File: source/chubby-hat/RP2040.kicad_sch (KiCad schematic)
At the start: 23 parts, among them U4 P25Q40H-SSH-IT, U5 RP2040, Y1 12M

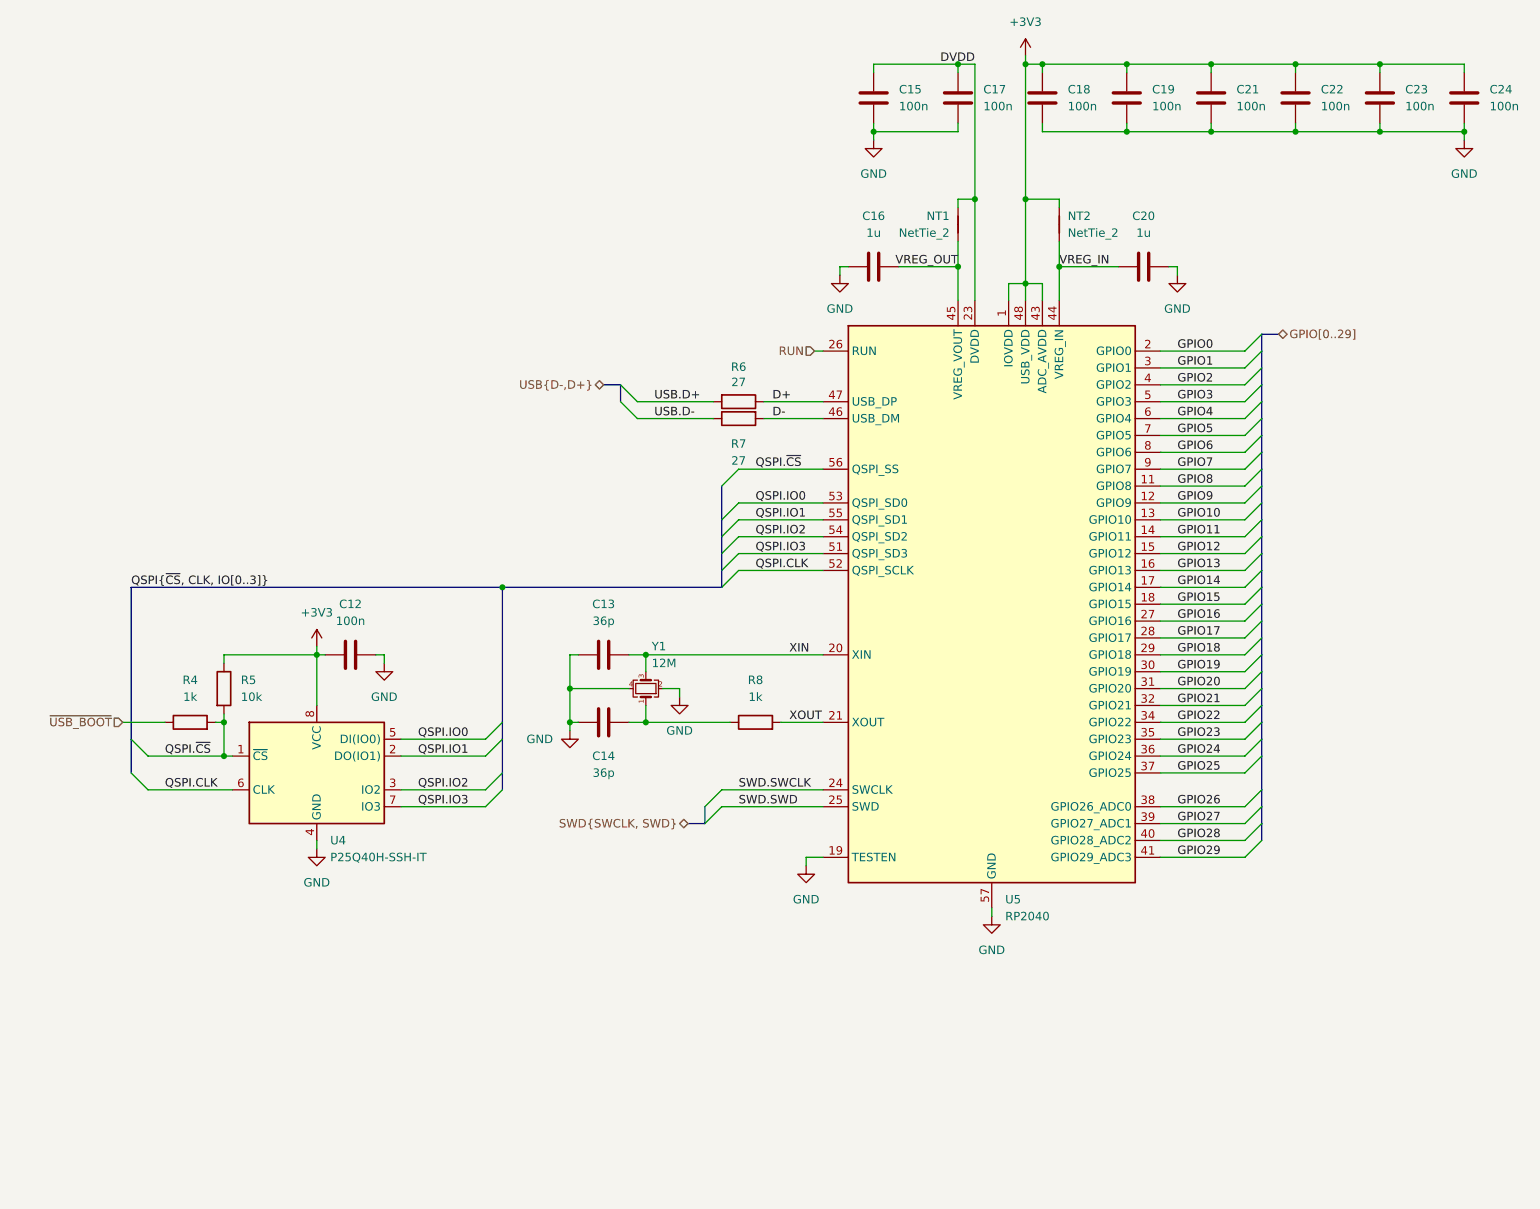
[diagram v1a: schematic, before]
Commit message: add test points and leds - closes #1; add fuse - closes #4; add silk screen art
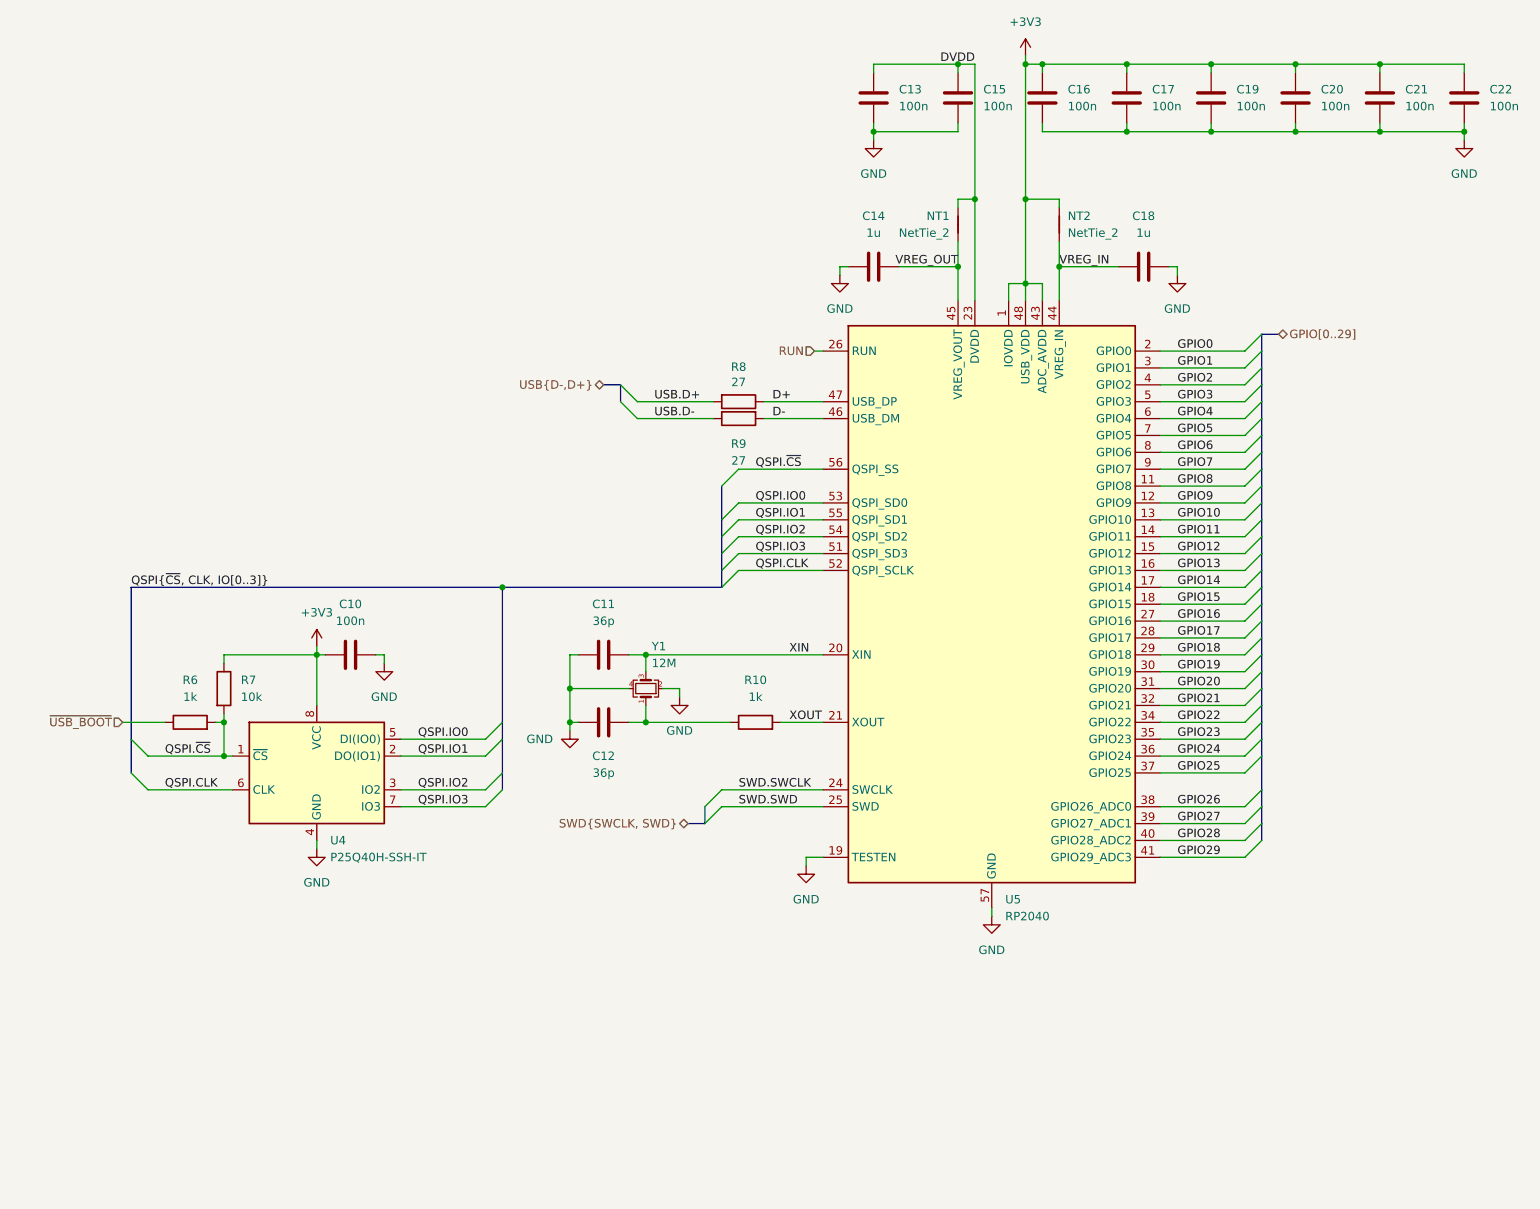
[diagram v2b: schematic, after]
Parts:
- renumbered C12 to C10, C13 to C11, C14 to C12, C15 to C13, C16 to C14, C17 to C15, C18 to C16, C19 to C17, C20 to C18, C21 to C19, C22 to C20, C23 to C21, C24 to C22, R8 to R10, R4 to R6, R5 to R7, R6 to R8, R7 to R9
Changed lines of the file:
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@@
   (symbol (lib_id "power:GND") (at 241.3 36.83 0) (unit 1)
     (in_bom yes) (on_board yes) (fields_autoplaced)
-    (property "Reference" "#PWR093" (id 0) (at 241.3 43.18 0)
+    (property "Reference" "#PWR096" (id 0) (at 241.3 43.18 0)
       (effects (font (size 1.27 1.27)) hide)
     )
@@
   (symbol (lib_id "Device:C") (at 73.66 114.3 90) (unit 1)
     (in_bom yes) (on_board yes) (fields_autoplaced)
-    (property "Reference" "C12" (id 0) (at 73.66 106.68 90))
+    (property "Reference" "C10" (id 0) (at 73.66 106.68 90))
     (property "Value" "100n" (id 1) (at 73.66 109.22 90))
     (property "Footprint" "Capacitor_SMD:C_0603_1608Metric" (id 2) (at 77.47 113.335 0)
@@
   (symbol (lib_id "Device:C") (at 152.4 30.48 0) (unit 1)
     (in_bom yes) (on_board yes) (fields_autoplaced)
-    (property "Reference" "C15" (id 0) (at 156.21 29.2099 0)
+    (property "Reference" "C13" (id 0) (at 156.21 29.2099 0)
       (effects (font (size 1.27 1.27)) (justify left))
     )
@@
   (symbol (lib_id "Device:C") (at 190.5 30.48 0) (unit 1)
     (in_bom yes) (on_board yes) (fields_autoplaced)
-    (property "Reference" "C19" (id 0) (at 194.31 29.2099 0)
+    (property "Reference" "C17" (id 0) (at 194.31 29.2099 0)
       (effects (font (size 1.27 1.27)) (justify left))
     )
@@
   (symbol (lib_id "power:+3V3") (at 68.58 113.03 0) (unit 1)
     (in_bom yes) (on_board yes) (fields_autoplaced)
-    (property "Reference" "#PWR082" (id 0) (at 68.58 116.84 0)
+    (property "Reference" "#PWR085" (id 0) (at 68.58 116.84 0)
       (effects (font (size 1.27 1.27)) hide)
     )
@@
   (symbol (lib_id "power:GND") (at 68.58 143.51 0) (unit 1)
     (in_bom yes) (on_board yes) (fields_autoplaced)
-    (property "Reference" "#PWR083" (id 0) (at 68.58 149.86 0)
+    (property "Reference" "#PWR086" (id 0) (at 68.58 149.86 0)
       (effects (font (size 1.27 1.27)) hide)
     )
@@
   (symbol (lib_id "power:GND") (at 147.32 57.15 0) (unit 1)
     (in_bom yes) (on_board yes) (fields_autoplaced)
-    (property "Reference" "#PWR088" (id 0) (at 147.32 63.5 0)
+    (property "Reference" "#PWR091" (id 0) (at 147.32 63.5 0)
       (effects (font (size 1.27 1.27)) hide)
     )
@@
   (symbol (lib_id "Device:C") (at 228.6 30.48 0) (unit 1)
     (in_bom yes) (on_board yes) (fields_autoplaced)
-    (property "Reference" "C23" (id 0) (at 232.41 29.2099 0)
+    (property "Reference" "C21" (id 0) (at 232.41 29.2099 0)
       (effects (font (size 1.27 1.27)) (justify left))
     )
@@
   (symbol (lib_id "power:GND") (at 152.4 36.83 0) (unit 1)
     (in_bom yes) (on_board yes) (fields_autoplaced)
-    (property "Reference" "#PWR089" (id 0) (at 152.4 43.18 0)
+    (property "Reference" "#PWR092" (id 0) (at 152.4 43.18 0)
       (effects (font (size 1.27 1.27)) hide)
     )
@@
   (symbol (lib_id "power:GND") (at 78.74 115.57 0) (unit 1)
     (in_bom yes) (on_board yes) (fields_autoplaced)
-    (property "Reference" "#PWR084" (id 0) (at 78.74 121.92 0)
+    (property "Reference" "#PWR087" (id 0) (at 78.74 121.92 0)
       (effects (font (size 1.27 1.27)) hide)
     )
@@
   (symbol (lib_id "Device:R") (at 49.53 124.46 90) (unit 1)
     (in_bom yes) (on_board yes) (fields_autoplaced)
-    (property "Reference" "R4" (id 0) (at 49.53 118.11 90))
+    (property "Reference" "R6" (id 0) (at 49.53 118.11 90))
     (property "Value" "1k" (id 1) (at 49.53 120.65 90))
     (property "Footprint" "Resistor_SMD:R_0603_1608Metric" (id 2) (at 49.53 126.238 90)
@@
   (symbol (lib_id "Device:C") (at 203.2 30.48 0) (unit 1)
     (in_bom yes) (on_board yes) (fields_autoplaced)
-    (property "Reference" "C21" (id 0) (at 207.01 29.2099 0)
+    (property "Reference" "C19" (id 0) (at 207.01 29.2099 0)
       (effects (font (size 1.27 1.27)) (justify left))
     )
@@
   (symbol (lib_id "power:+3V3") (at 175.26 24.13 0) (unit 1)
     (in_bom yes) (on_board yes) (fields_autoplaced)
-    (property "Reference" "#PWR091" (id 0) (at 175.26 27.94 0)
+    (property "Reference" "#PWR094" (id 0) (at 175.26 27.94 0)
       (effects (font (size 1.27 1.27)) hide)
     )
@@
   (symbol (lib_id "Device:C") (at 241.3 30.48 0) (unit 1)
     (in_bom yes) (on_board yes) (fields_autoplaced)
-    (property "Reference" "C24" (id 0) (at 245.11 29.2099 0)
+    (property "Reference" "C22" (id 0) (at 245.11 29.2099 0)
       (effects (font (size 1.27 1.27)) (justify left))
     )
@@
   (symbol (lib_id "Device:C") (at 152.4 55.88 270) (unit 1)
     (in_bom yes) (on_board yes) (fields_autoplaced)
-    (property "Reference" "C16" (id 0) (at 152.4 48.26 90))
+    (property "Reference" "C14" (id 0) (at 152.4 48.26 90))
     (property "Value" "1u" (id 1) (at 152.4 50.8 90))
     (property "Footprint" "Capacitor_SMD:C_0603_1608Metric" (id 2) (at 148.59 56.845 0)
@@
   (symbol (lib_id "Device:C") (at 165.1 30.48 0) (unit 1)
     (in_bom yes) (on_board yes) (fields_autoplaced)
-    (property "Reference" "C17" (id 0) (at 168.91 29.2099 0)
+    (property "Reference" "C15" (id 0) (at 168.91 29.2099 0)
       (effects (font (size 1.27 1.27)) (justify left))
     )
@@
   (symbol (lib_id "Device:C") (at 193.04 55.88 90) (unit 1)
     (in_bom yes) (on_board yes) (fields_autoplaced)
-    (property "Reference" "C20" (id 0) (at 193.04 48.26 90))
+    (property "Reference" "C18" (id 0) (at 193.04 48.26 90))
     (property "Value" "1u" (id 1) (at 193.04 50.8 90))
     (property "Footprint" "Capacitor_SMD:C_0603_1608Metric" (id 2) (at 196.85 54.915 0)
@@
   (symbol (lib_id "Device:C") (at 111.76 124.46 270) (mirror x) (unit 1)
     (in_bom yes) (on_board yes) (fields_autoplaced)
-    (property "Reference" "C14" (id 0) (at 111.76 129.54 90))
+    (property "Reference" "C12" (id 0) (at 111.76 129.54 90))
     (property "Value" "36p" (id 1) (at 111.76 132.08 90))
     (property "Footprint" "Capacitor_SMD:C_0603_1608Metric" (id 2) (at 107.95 123.495 0)
@@
   (symbol (lib_id "Device:R") (at 134.62 124.46 90) (unit 1)
     (in_bom yes) (on_board yes) (fields_autoplaced)
-    (property "Reference" "R8" (id 0) (at 134.62 118.11 90))
+    (property "Reference" "R10" (id 0) (at 134.62 118.11 90))
     (property "Value" "1k" (id 1) (at 134.62 120.65 90))
     (property "Footprint" "Resistor_SMD:R_0603_1608Metric" (id 2) (at 134.62 126.238 90)
@@
   (symbol (lib_id "power:GND") (at 123.19 120.65 0) (unit 1)
     (in_bom yes) (on_board yes) (fields_autoplaced)
-    (property "Reference" "#PWR086" (id 0) (at 123.19 127 0)
+    (property "Reference" "#PWR089" (id 0) (at 123.19 127 0)
       (effects (font (size 1.27 1.27)) hide)
     )
@@
   (symbol (lib_id "power:GND") (at 170.18 153.67 0) (unit 1)
     (in_bom yes) (on_board yes) (fields_autoplaced)
-    (property "Reference" "#PWR090" (id 0) (at 170.18 160.02 0)
+    (property "Reference" "#PWR093" (id 0) (at 170.18 160.02 0)
       (effects (font (size 1.27 1.27)) hide)
     )
@@
   (symbol (lib_id "Device:C") (at 215.9 30.48 0) (unit 1)
     (in_bom yes) (on_board yes) (fields_autoplaced)
-    (property "Reference" "C22" (id 0) (at 219.71 29.2099 0)
+    (property "Reference" "C20" (id 0) (at 219.71 29.2099 0)
       (effects (font (size 1.27 1.27)) (justify left))
     )
@@
   (symbol (lib_id "Device:C") (at 177.8 30.48 0) (unit 1)
     (in_bom yes) (on_board yes) (fields_autoplaced)
-    (property "Reference" "C18" (id 0) (at 181.61 29.2099 0)
+    (property "Reference" "C16" (id 0) (at 181.61 29.2099 0)
       (effects (font (size 1.27 1.27)) (justify left))
     )
@@
   (symbol (lib_id "power:GND") (at 198.12 57.15 0) (unit 1)
     (in_bom yes) (on_board yes) (fields_autoplaced)
-    (property "Reference" "#PWR092" (id 0) (at 198.12 63.5 0)
+    (property "Reference" "#PWR095" (id 0) (at 198.12 63.5 0)
       (effects (font (size 1.27 1.27)) hide)
     )
@@
   (symbol (lib_id "power:GND") (at 106.68 125.73 0) (unit 1)
     (in_bom yes) (on_board yes) (fields_autoplaced)
-    (property "Reference" "#PWR085" (id 0) (at 106.68 132.08 0)
+    (property "Reference" "#PWR088" (id 0) (at 106.68 132.08 0)
       (effects (font (size 1.27 1.27)) hide)
     )
@@
   (symbol (lib_id "Device:C") (at 111.76 114.3 270) (mirror x) (unit 1)
     (in_bom yes) (on_board yes) (fields_autoplaced)
-    (property "Reference" "C13" (id 0) (at 111.76 106.68 90))
+    (property "Reference" "C11" (id 0) (at 111.76 106.68 90))
     (property "Value" "36p" (id 1) (at 111.76 109.22 90))
     (property "Footprint" "Capacitor_SMD:C_0603_1608Metric" (id 2) (at 107.95 113.335 0)
@@
   (symbol (lib_id "Device:R") (at 132.08 76.2 270) (unit 1)
     (in_bom yes) (on_board yes)
-    (property "Reference" "R6" (id 0) (at 132.08 70.9738 90))
+    (property "Reference" "R8" (id 0) (at 132.08 70.9738 90))
     (property "Value" "27" (id 1) (at 132.08 73.2725 90))
     (property "Footprint" "Resistor_SMD:R_0603_1608Metric" (id 2) (at 132.08 74.422 90)
@@
   (symbol (lib_id "Device:R") (at 132.08 78.74 90) (mirror x) (unit 1)
     (in_bom yes) (on_board yes)
-    (property "Reference" "R7" (id 0) (at 132.08 82.55 90))
+    (property "Reference" "R9" (id 0) (at 132.08 82.55 90))
     (property "Value" "27" (id 1) (at 132.08 85.09 90))
     (property "Footprint" "Resistor_SMD:R_0603_1608Metric" (id 2) (at 132.08 76.962 90)
@@
   (symbol (lib_id "Device:R") (at 54.61 119.38 0) (unit 1)
     (in_bom yes) (on_board yes) (fields_autoplaced)
-    (property "Reference" "R5" (id 0) (at 57.15 118.1099 0)
+    (property "Reference" "R7" (id 0) (at 57.15 118.1099 0)
       (effects (font (size 1.27 1.27)) (justify left))
     )
@@
   (symbol (lib_id "power:GND") (at 142.24 146.05 0) (unit 1)
     (in_bom yes) (on_board yes) (fields_autoplaced)
-    (property "Reference" "#PWR087" (id 0) (at 142.24 152.4 0)
-      (effects (font (size 1.27 1.27)) hide)
-    )
+    (property "Reference" "#PWR090" (id 0) (at 142.24 152.4 0)
+      (effects (font (size 1.27 1.27)) hide)
+    )
